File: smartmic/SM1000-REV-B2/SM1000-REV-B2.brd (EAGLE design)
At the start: 65 x 90 mm, 175 parts, among them CN1 HDR100-3, CN10 MJ-3523-SMT, CN11 HDR100-3, CN12 DF11-16DS, CN2 MOLEX-MINI-B-SMT, CN3 RASM712PX, CN4 RJ-45, CN5 MJ-3523-SMT, CN6 MJ-3523-SMT, CN7 MJ-3523-SMT, CN8 MJ-3523-SMT, CN9 MJ-3523-SMT, J1 JMP-2PIN, J3 JMP-2PIN, J4 JMP-2PIN, J5 JMP-2PIN, P1 TPAD50, P10 TPAD50, P11 TPAD50, P12 TPAD50, P13 TPAD50, P14 TPAD50, P15 TPAD50, P16 TPAD50, P17 TPAD50, P18 TPAD50, P19 TPAD50, P2 TPAD50, P20 TPAD50, P3 TPAD50, P4 TPAD50, P5 TPAD50, P6 TPAD50, P7 TPAD50, P8 TPAD50, P9 TPAD50, SW1 SW-BOURNS-7914S, SW2 SW-BOURNS-7914S, SW3 DPDT, SW4 SW-BOURNS-7914S, T1 SM-LP-5001, T2 SM-LP-5001, U1 STM32F405, U2 LD3985M33R, U3 STMPS2141, U4 EMIF02-USB03F2, U5 TPS54329E, U6 LMV341, U7 LMV341, U8 LM386M-1, U9 LMV341

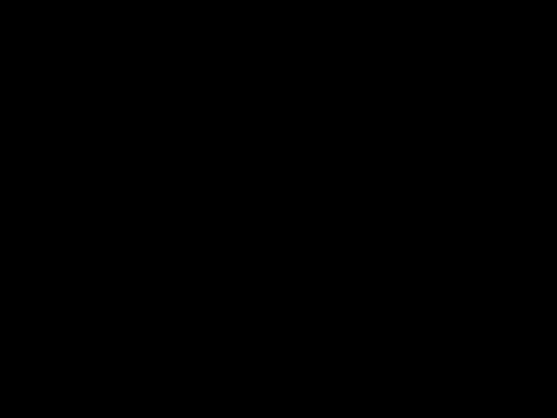
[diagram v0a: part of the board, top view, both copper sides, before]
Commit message: Implemented Davids changes(21, 22 & 23) to schematic. Parts are in PCB, but not placed. RGB Updated Change Log RGB
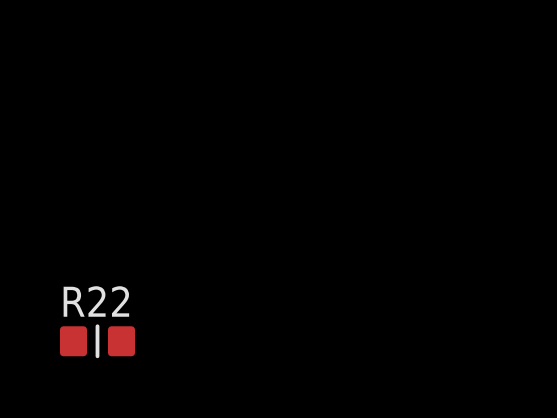
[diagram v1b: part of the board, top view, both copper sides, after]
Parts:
- added R22: 22.1K,1%, AA-ipc-7351-resistor:RESC1608X55N
- R46: value 10K -> 100K
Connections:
- net DAC2_OUT: now also R22.2
- net GND: now also R22.1
